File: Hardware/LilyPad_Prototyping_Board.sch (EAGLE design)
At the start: 138 parts, among them J1 SEWTAP_LONG-2SIDE, J10 SEWTAP_LONG-2SIDE, J11 SEWTAP_LONG-2SIDE, J12 SEWTAP_LONG-2SIDE, J13 SEWTAP_LONG-2SIDE, J14 SEWTAP_LONG-2SIDE, J15 AMP FCI 10103594-0001LF, J2 SEWTAP_LONG-2SIDE, J3 SEWTAP_LONG-2SIDE, J4 SEWTAP_LONG-2SIDE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

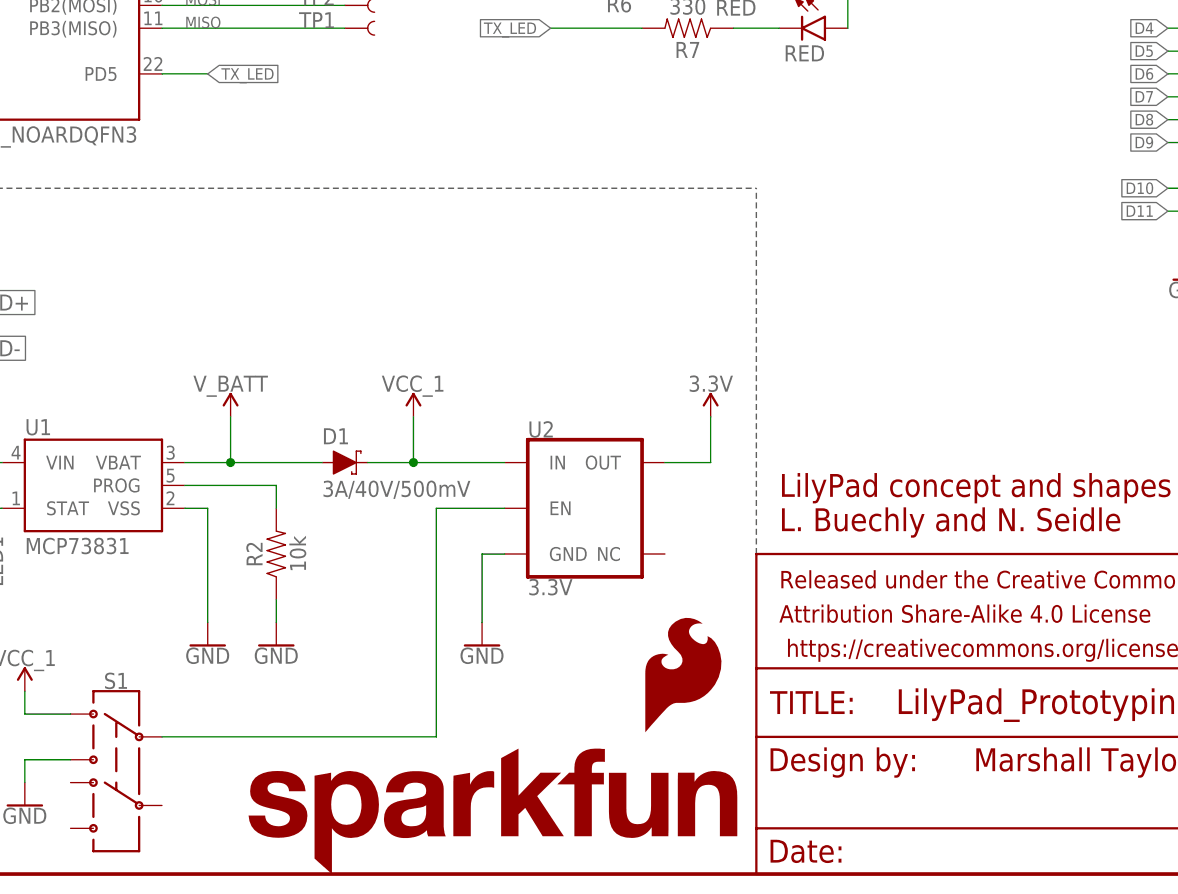
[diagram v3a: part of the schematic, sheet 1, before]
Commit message: Added extra test points
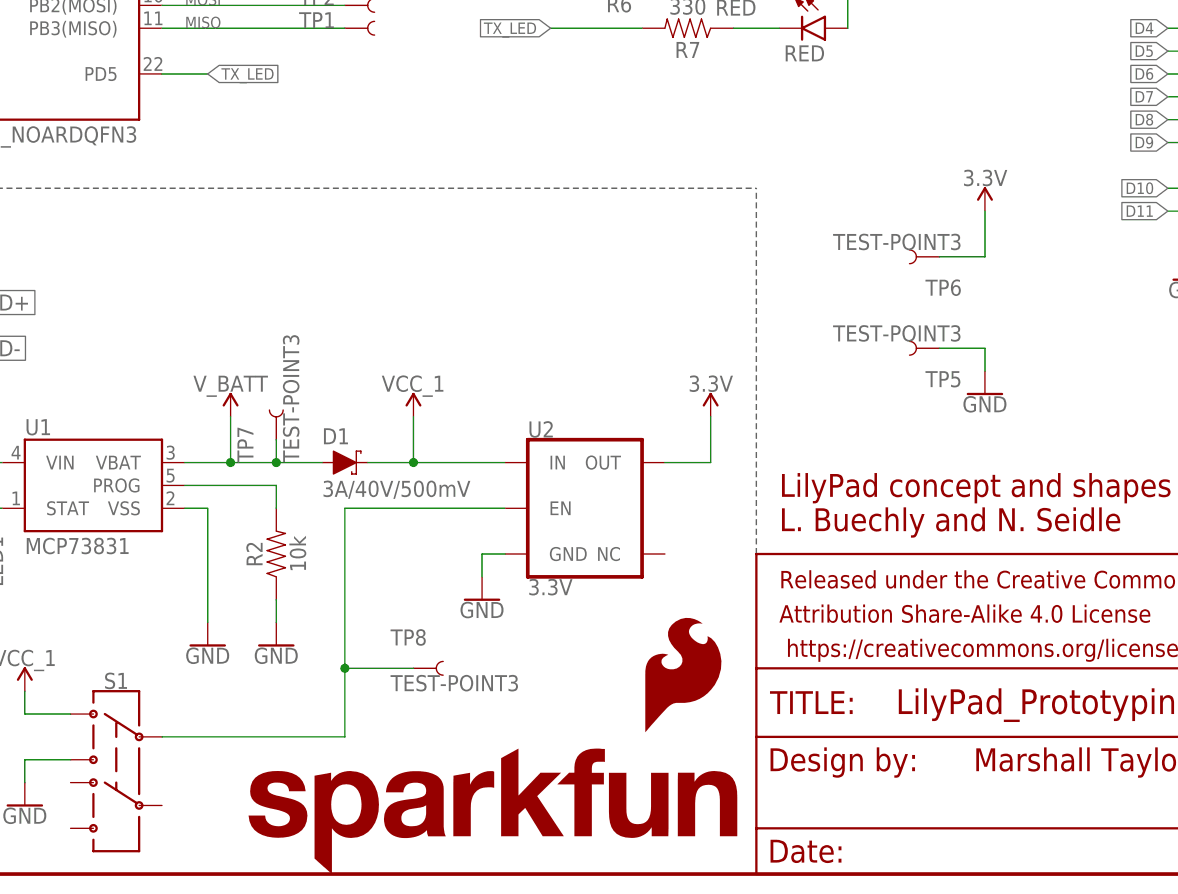
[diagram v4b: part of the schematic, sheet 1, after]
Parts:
- added TP5, TP6, TP7, TP8: TEST-POINT3, SparkFun-Connectors:TEST-POINT3
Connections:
- net 3.3V: now also TP6.1
- net GND: now also TP5.1
- net N$2: now also TP8.1
- net V_BATT: now also TP7.1
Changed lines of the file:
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@@
 <part name="LOGO6" library="SparkFun-Aesthetics" deviceset="OSHW-LOGO" device="S"/>
 <part name="D10" library="newLilypadParts" deviceset="SUNLED" device="SMD1" value="XZM2CRKM2DGFBB45SCCB"/>
+<part name="TP5" library="SparkFun-Connectors" deviceset="TEST-POINT" device="3"/>
+<part name="TP6" library="SparkFun-Connectors" deviceset="TEST-POINT" device="3"/>
+<part name="GND28" library="SparkFun-PowerSymbols" deviceset="GND" device=""/>
+<part name="P+9" library="SparkFun-PowerSymbols" deviceset="3.3V" device=""/>
+<part name="TP7" library="SparkFun-Connectors" deviceset="TEST-POINT" device="3"/>
+<part name="TP8" library="SparkFun-Connectors" deviceset="TEST-POINT" device="3"/>
 </parts>
 <sheets>
@@
 <instance part="U$2" gate="G$1" x="233.68" y="175.26"/>
 <instance part="U2" gate="G$1" x="129.54" y="40.64"/>
-<instance part="GND4" gate="1" x="116.84" y="25.4"/>
+<instance part="GND4" gate="1" x="116.84" y="30.48"/>
 <instance part="GND15" gate="1" x="93.98" y="25.4"/>
 <instance part="TP1" gate="G$1" x="101.6" y="93.98" smashed="yes">
@@
 <instance part="LOGO6" gate="G$1" x="233.68" y="53.34"/>
 <instance part="D10" gate="G1" x="157.48" y="157.48"/>
+<instance part="TP5" gate="G$1" x="167.64" y="58.42" rot="R180"/>
+<instance part="TP6" gate="G$1" x="167.64" y="68.58" rot="R180"/>
+<instance part="GND28" gate="1" x="172.72" y="53.34"/>
+<instance part="P+9" gate="G$1" x="172.72" y="73.66"/>
+<instance part="TP7" gate="G$1" x="93.98" y="48.26" rot="R90"/>
+<instance part="TP8" gate="G$1" x="109.22" y="22.86"/>
 </instances>
 <busses>
@@
 <segment>
 <pinref part="S1" gate="G$1" pin="2"/>
-<wire x1="81.28" y1="15.24" x2="111.76" y2="15.24" width="0.1524" layer="91"/>
-<wire x1="111.76" y1="15.24" x2="111.76" y2="40.64" width="0.1524" layer="91"/>
-<wire x1="111.76" y1="40.64" x2="119.38" y2="40.64" width="0.1524" layer="91"/>
+<wire x1="81.28" y1="15.24" x2="101.6" y2="15.24" width="0.1524" layer="91"/>
+<wire x1="101.6" y1="15.24" x2="101.6" y2="22.86" width="0.1524" layer="91"/>
+<wire x1="101.6" y1="22.86" x2="101.6" y2="40.64" width="0.1524" layer="91"/>
+<wire x1="101.6" y1="40.64" x2="119.38" y2="40.64" width="0.1524" layer="91"/>
 <pinref part="U2" gate="G$1" pin="EN"/>
+<junction x="101.6" y="22.86"/>
+<pinref part="TP8" gate="G$1" pin="1"/>
+<wire x1="109.22" y1="22.86" x2="101.6" y2="22.86" width="0.1524" layer="91"/>
 </segment>
 </net>
@@
 <wire x1="88.9" y1="50.8" x2="88.9" y2="45.72" width="0.1524" layer="91"/>
 <pinref part="D1" gate="G$1" pin="A"/>
-<wire x1="99.06" y1="45.72" x2="88.9" y2="45.72" width="0.1524" layer="91"/>
+<wire x1="99.06" y1="45.72" x2="93.98" y2="45.72" width="0.1524" layer="91"/>
 <junction x="88.9" y="45.72"/>
+<junction x="93.98" y="45.72"/>
+<wire x1="93.98" y1="45.72" x2="88.9" y2="45.72" width="0.1524" layer="91"/>
+<pinref part="TP7" gate="G$1" pin="1"/>
+<wire x1="93.98" y1="45.72" x2="93.98" y2="48.26" width="0.1524" layer="91"/>
 </segment>
 <segment>
@@
 <pinref part="GND4" gate="1" pin="GND"/>
 <wire x1="119.38" y1="35.56" x2="116.84" y2="35.56" width="0.1524" layer="91"/>
-<wire x1="116.84" y1="35.56" x2="116.84" y2="27.94" width="0.1524" layer="91"/>
+<wire x1="116.84" y1="35.56" x2="116.84" y2="33.02" width="0.1524" layer="91"/>
 </segment>
 <segment>
@@
 <wire x1="93.98" y1="30.48" x2="93.98" y2="27.94" width="0.1524" layer="91"/>
 <pinref part="GND15" gate="1" pin="GND"/>
+</segment>
+<segment>
+<pinref part="TP5" gate="G$1" pin="1"/>
+<pinref part="GND28" gate="1" pin="GND"/>
+<wire x1="167.64" y1="58.42" x2="172.72" y2="58.42" width="0.1524" layer="91"/>
+<wire x1="172.72" y1="58.42" x2="172.72" y2="55.88" width="0.1524" layer="91"/>
 </segment>
 </net>
@@
 <pinref part="P+5" gate="G$1" pin="3.3V"/>
 </segment>
-</net>
+<segment>
+<pinref part="TP6" gate="G$1" pin="1"/>
+<pinref part="P+9" gate="G$1" pin="3.3V"/>
+<wire x1="167.64" y1="68.58" x2="172.72" y2="68.58" width="0.1524" layer="91"/>
+<wire x1="172.72" y1="68.58" x2="172.72" y2="73.66" width="0.1524" layer="91"/>
+</segment>
+</net>

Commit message: Adjusted routes, drills, and USB connector for PCB fab house requirements, incremented design to v03
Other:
- note added: "v03"
- note removed: "v01"
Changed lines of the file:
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@@
 <text x="220.98" y="151.13" size="1.27" layer="97">MIC5219 BYPASS</text>
 <text x="171.45" y="11.43" size="2.54" layer="94">Marshall Taylor</text>
-<text x="238.252" y="7.112" size="2.54" layer="94">v01</text>
+<text x="238.252" y="7.112" size="2.54" layer="94">v03</text>
 <text x="149.86" y="38.1" size="2.54" layer="94">LilyPad concept and shapes by:
 L. Buechly and N. Seidle</text>
@@
 <text x="53.34" y="86.36" size="1.778" layer="97">Buzzer</text>
 <text x="171.45" y="11.43" size="2.54" layer="94">Marshall Taylor</text>
-<text x="238.252" y="7.112" size="2.54" layer="94">v01</text>
+<text x="238.252" y="7.112" size="2.54" layer="94">v03</text>
 <text x="60.96" y="25.4" size="1.778" layer="97">Un-used
 sew taps</text>

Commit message: Implemented most physical changes from proto 1
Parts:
- S4: value MOMENTARY-SWITCH-SPST-SMD-4.6X2.8MM -> MOMENTARY-SWITCH-SPST-SMD-5.2-REDUNDANT; device SparkFun-Switches:MOMENTARY-SWITCH-SPST-SMD-4.6X2.8MM -> SparkFun-Switches:MOMENTARY-SWITCH-SPST-SMD-5.2-REDUNDANT
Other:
- note added: "v10"
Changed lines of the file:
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@@
 <part name="GND24" library="SparkFun-PowerSymbols" deviceset="GND" device=""/>
 <part name="GND25" library="SparkFun-PowerSymbols" deviceset="GND" device=""/>
-<part name="S4" library="SparkFun-Switches" deviceset="MOMENTARY-SWITCH-SPST" device="-SMD-4.6X2.8MM" value="MOMENTARY-SWITCH-SPST-SMD-4.6X2.8MM"/>
+<part name="S4" library="SparkFun-Switches" deviceset="MOMENTARY-SWITCH-SPST" device="-SMD-5.2-REDUNDANT" value="MOMENTARY-SWITCH-SPST-SMD-5.2-REDUNDANT"/>
 <part name="U$52/SCL1" library="newLilypadParts" deviceset="GATOR_HOLE_PAIR" device=""/>
 <part name="FRAME2" library="SparkFun-Aesthetics" deviceset="FRAME-LETTER" device="NO_PACKAGE"/>
@@
 <text x="220.98" y="151.13" size="1.27" layer="97">MIC5219 BYPASS</text>
 <text x="171.45" y="11.43" size="2.54" layer="94">Marshall Taylor</text>
-<text x="238.252" y="7.112" size="2.54" layer="94">v03</text>
+<text x="238.252" y="7.112" size="2.54" layer="94">v10</text>
 <text x="149.86" y="38.1" size="2.54" layer="94">LilyPad concept and shapes by:
 L. Buechly and N. Seidle</text>

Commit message: More proto changes in
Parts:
- removed U$43, U$72: LILYLOGO_ABR, newLilypadParts:LILYLOGO_ABR
- LED2: value RED -> Yellow; device SparkFun-LED:LED-RED0603 -> SparkFun-LED:LED-YELLOW0603; PROD_ID DIO-00819 -> (none)
- LED3: value RED -> GREEN; device SparkFun-LED:LED-RED0603 -> SparkFun-LED:LED-GREEN0603
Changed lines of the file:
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@@
 <attribute name="PROD_ID" value="RES-00818"/>
 </part>
-<part name="LED2" library="SparkFun-LED" deviceset="LED-RED" device="0603" value="RED">
-<attribute name="PROD_ID" value="DIO-00819"/>
-</part>
-<part name="LED3" library="SparkFun-LED" deviceset="LED-RED" device="0603" value="RED">
+<part name="LED2" library="SparkFun-LED" deviceset="LED-YELLOW" device="0603" value="Yellow"/>
+<part name="LED3" library="SparkFun-LED" deviceset="LED-GREEN" device="0603" value="GREEN">
 <attribute name="PROD_ID" value="DIO-00819"/>
 </part>
@@
 <part name="GND27" library="SparkFun-PowerSymbols" deviceset="GND" device=""/>
 <part name="U$1" library="newLilypadParts" deviceset="LILYLOGO_SHORT" device=""/>
-<part name="U$43" library="newLilypadParts" deviceset="LILYLOGO_ABR" device=""/>
-<part name="U$72" library="newLilypadParts" deviceset="LILYLOGO_ABR" device=""/>
 <part name="U$73" library="newLilypadParts" deviceset="LILYLOGO_ABR" device=""/>
 <part name="JP11" library="SparkFun" deviceset="FIDUCIAL" device="UFIDUCIAL"/>
@@
 <instance part="LOGO2" gate="G$1" x="134.62" y="15.24"/>
 <instance part="U$1" gate="G$1" x="220.98" y="38.1"/>
-<instance part="U$43" gate="G$1" x="236.22" y="38.1"/>
-<instance part="U$72" gate="G$1" x="236.22" y="38.1"/>
 <instance part="U$73" gate="G$1" x="236.22" y="38.1"/>
 <instance part="JP11" gate="G$1" x="236.22" y="25.4"/>

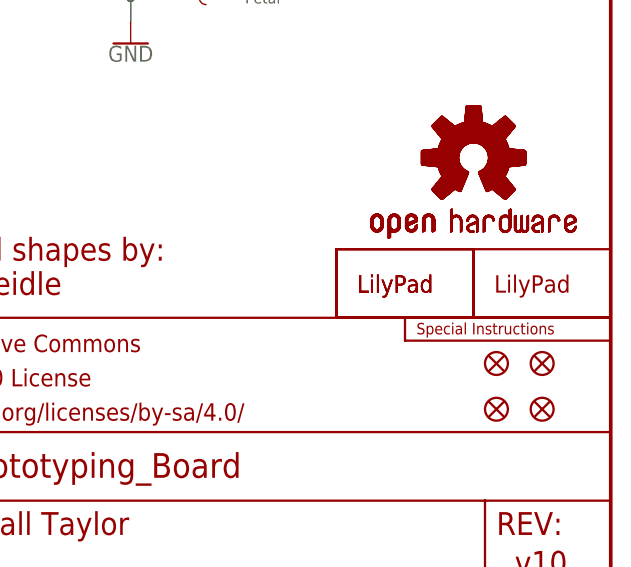
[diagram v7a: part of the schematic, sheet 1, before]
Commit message: Imported new silk
Replaced name and major labeling with polygons derived from Trebuchet
font (LilyPad standard). Polarity and internal labeling left in Eagle
vector font.
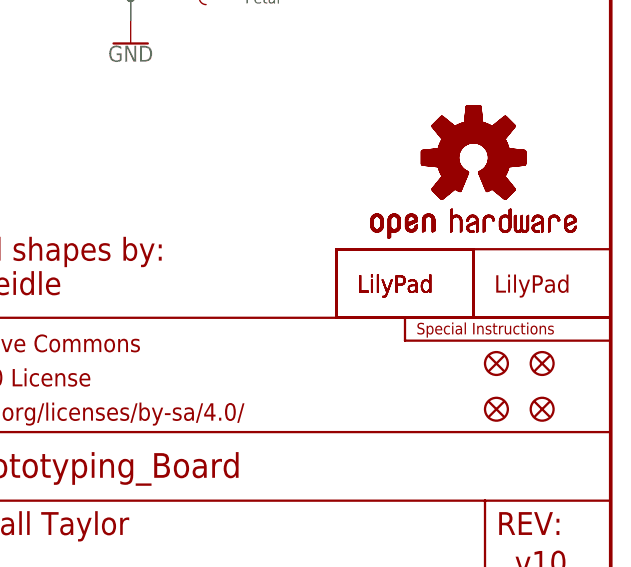
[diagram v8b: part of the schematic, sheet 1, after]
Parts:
- added U$43: LILYLOGO_SHORT, newLilypadParts:LILYLOGO_SHORT
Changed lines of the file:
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@@
 <?xml version="1.0" encoding="utf-8"?>
 <!DOCTYPE eagle SYSTEM "eagle.dtd">
-<eagle version="7.7.0">
+<eagle version="7.4.0">
 <drawing>
 <settings>
@@
 <part name="TP7" library="SparkFun-Connectors" deviceset="TEST-POINT" device="3"/>
 <part name="TP8" library="SparkFun-Connectors" deviceset="TEST-POINT" device="3"/>
+<part name="U$43" library="newLilypadParts" deviceset="LILYLOGO_SHORT" device=""/>
 </parts>
 <sheets>
@@
 <instance part="TP7" gate="G$1" x="93.98" y="48.26" rot="R90"/>
 <instance part="TP8" gate="G$1" x="109.22" y="22.86"/>
+<instance part="U$43" gate="G$1" x="220.98" y="38.1"/>
 </instances>
 <busses>
